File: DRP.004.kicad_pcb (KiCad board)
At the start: 4 copper layers, 55 x 27 mm, 80 parts, among them J1 Batt_conn_3p, J2 USB_C_Receptacle_PowerOnly_6P, J3 Conn_01x03_Pin, J4 Conn_01x05_Pin, J5 Conn_01x03_Pin, J6 Conn_01x03_Pin, Q1 DTC143Z, Q2 AO3400, Q3 DTC143Z, Q4 DMG1012T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

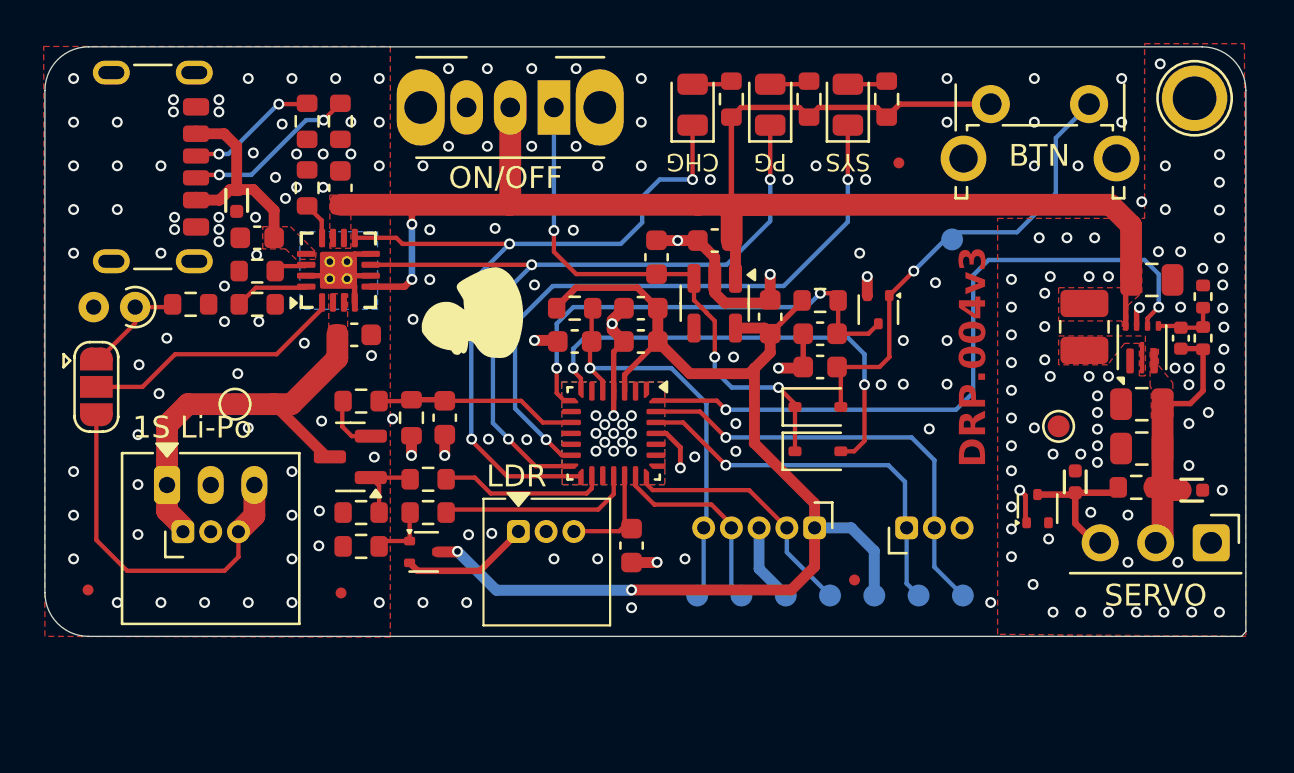
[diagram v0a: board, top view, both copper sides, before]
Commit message: Updated project jobset - Added generation of ibom - Updated production files
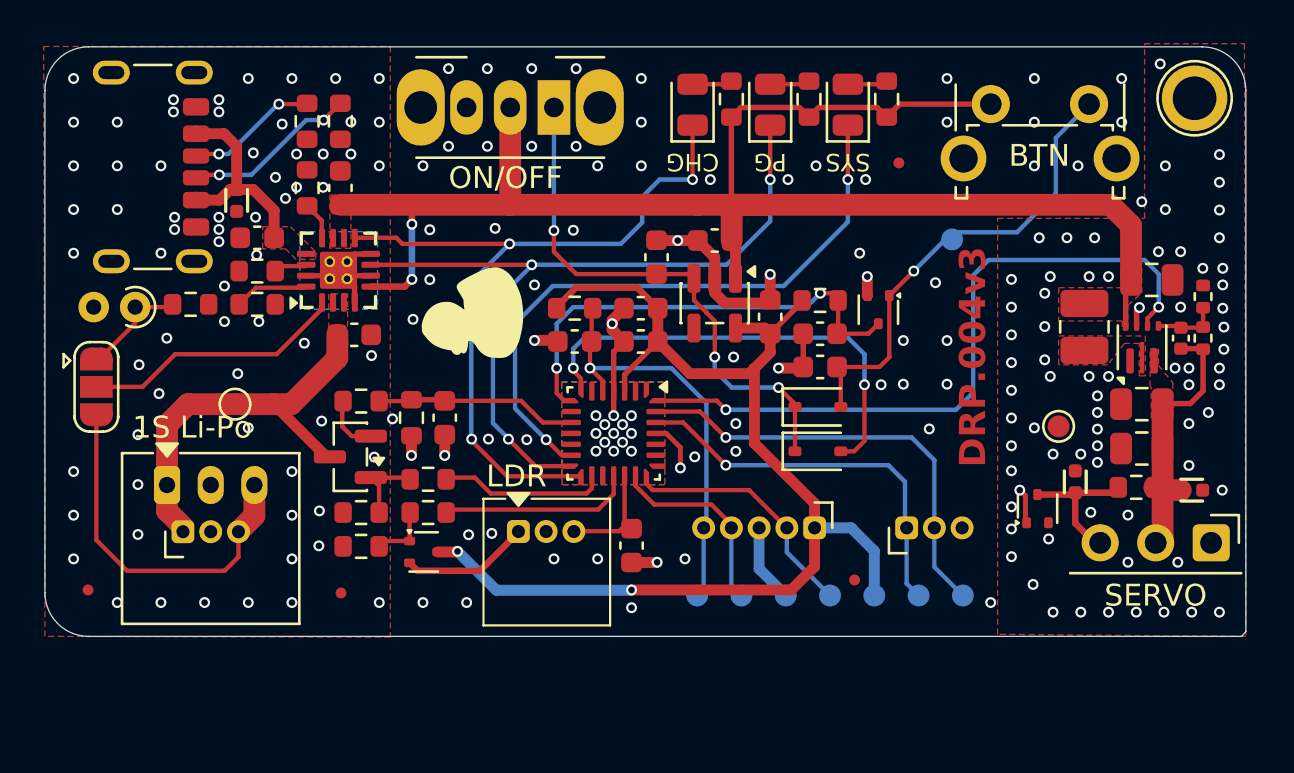
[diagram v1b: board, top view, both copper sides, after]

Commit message: V4 revision - Moved usb to HID side - Changed battery connector to ph2.0 with standard(ish) pinout - Better footprints for debug and ldr connectors - Changed switch from SK12D07 to MSK12C02 - Changed R(ILIM) to 1.1k - Better placement of servo power and connector - Changed thermistor to 0402 SMD - Removed jumper to NTC
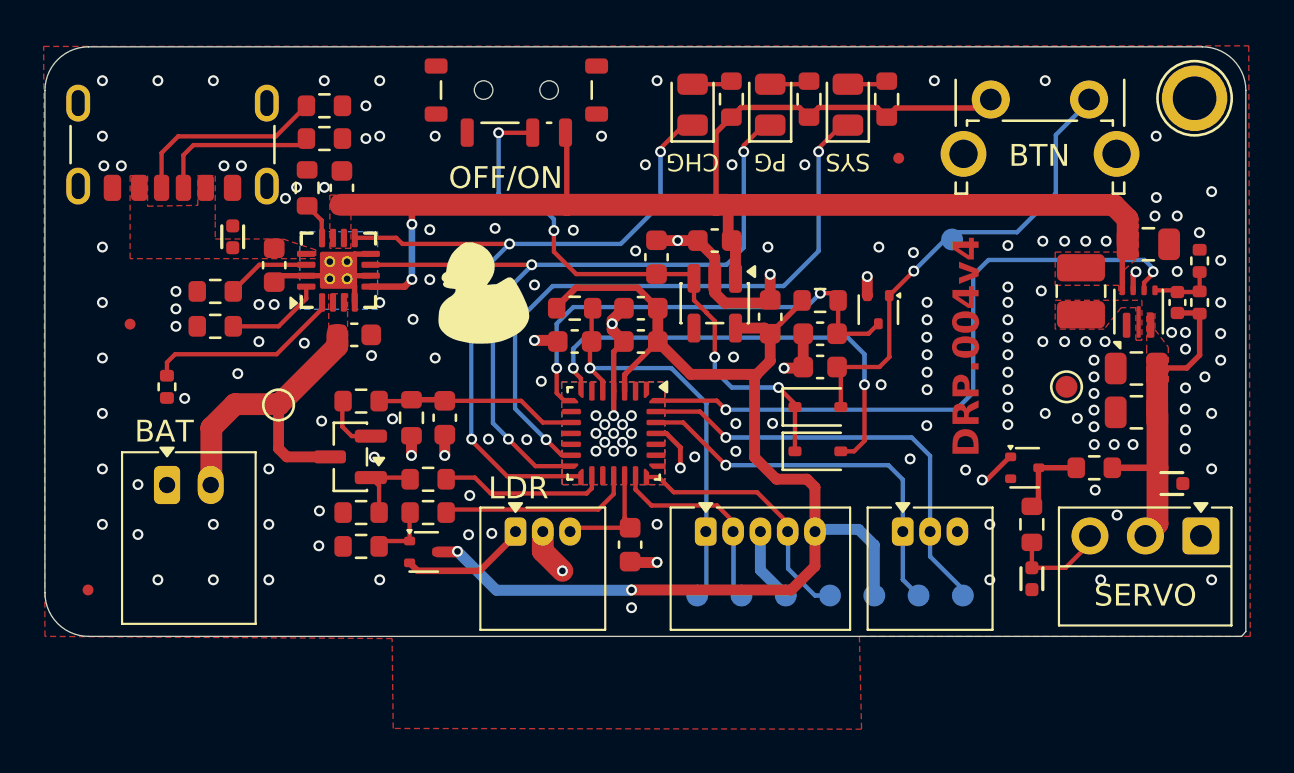
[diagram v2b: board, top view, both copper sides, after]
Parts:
- removed FID4: Fiducial, Fiducial:Fiducial_0.5mm_Mask1.5mm
- removed JP1: SolderJumper_3_Open, Jumper:SolderJumper-3_P1.3mm_Open_RoundedPad1.0x1.5mm
- removed Q1: DTC143Z, Muffin_SMD:SOT-523
- removed SW3: SW_SPDT, Button_Switch_THT:SW_Slide_SPDT_Angled_CK_OS102011MA1Q
- added Q6: DTC143Z, Muffin_SMD:SOT-523, F.Cu at (201.9, 90.3)
- added SW1: SW_SPDT_SH, Muffin_SMD:MSK12C02, F.Cu at (178.6, 73.0)
- J1: value Batt_conn_3p -> Conn_01x02_Pin; footprint Connector_Muffin_THT.pretty:BATTERY_P2+P1.27mm_Horizontal -> Connector_Muffin_THT.pretty:JST_PH_S2B-PH-K_1x02_P2.00mm_Horizontal
- J4: footprint Connector_Muffin_THT.pretty:PinHeader_1x05_P1.27mm_Vertical_clear_silk -> Connector_Muffin_THT.pretty:Molex_PicoBlade_53048-0510_1x05_P1.25mm_Horizontal
- J5: footprint Connector_Muffin_THT.pretty:PinHeader_1x03_P1.27mm_Vertical_clear_silk -> Connector_Muffin_THT.pretty:Molex_PicoBlade_53048-0310_1x03_P1.25mm_Horizontal
- J6: footprint Connector_Muffin_THT.pretty:Connector_JST_1x03_P1.27mm -> Connector_Muffin_THT.pretty:Molex_PicoBlade_53048-0310_1x03_P1.25mm_Horizontal
- R3: value 1.8k -> 1.1k
- R7: value 5.1k -> 100
- R9: value 10k -> 5.1k
- TH1: footprint Resistor_THT:R_Axial_DIN0204_L3.6mm_D1.6mm_P1.90mm_Vertical -> Resistor_SMD:R_0402_1005Metric
- moved R9 42.1 mm to (205.1, 90.3)
- moved FID2 19.4 mm to (196.1, 76.1)
- moved FID3 15.6 mm to (160.9, 83.7)
- moved R7 5.07 mm to (202.2, 92.9), turned to 90 degrees
- moved J4 4.98 mm to (187.3, 93.2), turned to 0 degrees
- moved U3 4.86 mm to (202.2, 95.4), turned to -90 degrees
- moved TH1 3.93 mm to (162.6, 86.6), turned to -90 degrees
- moved J2 2.92 mm to (162.8, 74.4), turned to 180 degrees
- moved R5 2.17 mm to (164.8, 83.8), turned to 180 degrees
- moved R4 2.13 mm to (164.8, 82.2)
- moved TP3 2.00 mm to (167.7, 87.4)
- moved TP7 1.85 mm to (203.8, 86.6)
- moved C3 1.68 mm to (207.0, 87.7)
- moved U4 1.67 mm to (165.6, 79.7), turned to 90 degrees
- moved C4 1.65 mm to (207.0, 85.7)
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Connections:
- J1 pad 1: +BATT -> GND
- J1 pad 2: GND -> +BATT
- J4 pad 1: +1V8 -> NRST
- J4 pad 2: SWCLK -> SWDIO
- J4 pad 4: SWDIO -> SWCLK
- J4 pad 5: NRST -> +1V8
- R7 pad 1: +5V5 -> Net-(J3-Pin_3)
- R7 pad 2: Net-(J3-Pin_3) -> /power/servo_cntrl
- R9 pad 1: GND -> +5V5
- R9 pad 2: Net-(JP1-A) -> /power/servo_cntrl
- TH1 pad 1: Net-(JP1-A) -> Net-(U1-TS)
- U1 pad 1: TS -> Net-(U1-TS)
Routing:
- net Net-(J1-TS): track 16.9 -> 0.00 mm
- net TS: track 11.8 -> 0.00 mm
- net VBUS: track 9.62 -> 0.00 mm
- net Net-(U1-TS): track 0.00 -> 8.73 mm
- net +BATT: track 19.7 -> 14.8 mm
- net Net-(JP1-A): track 4.77 -> 0.00 mm
- net VSYS: track 72.4 -> 68.3 mm
- net /power/servo_cntrl: track 0.00 -> 3.45 mm
- net Net-(U1-TMR): track 1.22 -> 3.84 mm
- net EN_SYS: track 24.2 -> 26.5 mm, vias 3 -> 4
- net +5V5: track 12.8 -> 14.7 mm
- net EN_SERVO: track 32.0 -> 30.2 mm
- net Net-(J3-Pin_3): track 6.15 -> 4.63 mm
- net Net-(J2-CC1): track 5.95 -> 7.45 mm, vias 2 -> 0
- net SERVO_PWM: track 19.9 -> 18.5 mm
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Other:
- board text added: "BAT"
- board text added: "OFF/ON"
- board text removed: "1S Li-Po"
- board text removed: "ON/OFF"

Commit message: v4.1 - Changed SW2 to SMT (with lower profile) - Widen annular ring of vias - Small changes in routing (due to wider vias)
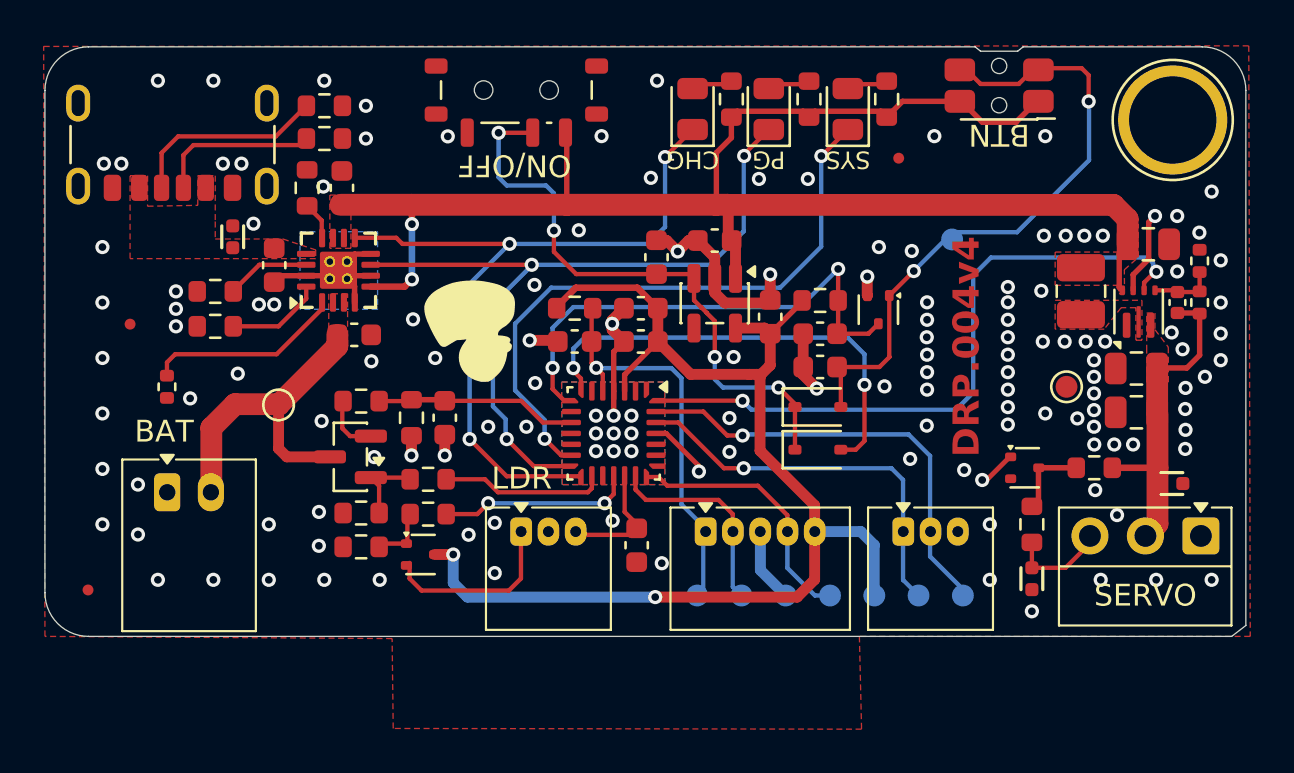
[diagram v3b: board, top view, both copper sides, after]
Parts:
- C16, C9: value 10nF -> 1nF
- R20, R21, R23: value 220 -> 1.1k
- SW2: footprint Button_Switch_THT:SW_Tactile_SPST_Angled_PTS645Vx58-2LFS -> Button_Switch_SMD:SW_SPST_EVQP7C
- TP6: footprint TestPoint:TestPoint_Plated_Hole_D2.0mm -> TestPoint:TestPoint_Plated_Hole_D4.0mm
- moved #G1 1.86 mm to (176.4, 84.0), turned to 180 degrees
- moved TP6 1.41 mm to (208.7, 74.3)
- moved SW2 0.74 mm to (200.7, 72.8), turned to 180 degrees
- moved J1 0.33 mm to (162.6, 91.4)
- moved C16 0.30 mm to (184.1, 93.8)
- moved J6 0.26 mm to (178.8, 93.2)
- moved D4 0.21 mm to (190.2, 73.8)
- moved D3 0.20 mm to (186.7, 73.8)
- moved D5 0.20 mm to (193.8, 73.8)
- moved Q4 0.19 mm to (174.2, 94.2)
- moved D1 0.07 mm to (192.4, 89.5)
- moved R22 0.07 mm to (174.6, 92.4)
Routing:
- net /control/SWITCH: track 21.2 -> 28.9 mm, vias 1 -> 2
- net VSYS: track 68.3 -> 71.2 mm
- net Net-(J6-Pin_1): track 5.86 -> 8.76 mm
- net ON_DETECT: track 20.8 -> 22.7 mm
- net +1V8: track 55.4 -> 56.6 mm
- net ADC_LDR: track 4.93 -> 5.91 mm
- net PGOOD: track 36.1 -> 35.2 mm
- net CHRG: track 34.4 -> 35.1 mm
- net GND: track 34.1 -> 34.7 mm, vias 169 -> 141
- net SWDIO: track 8.87 -> 9.45 mm
- net EN_LDR: track 8.75 -> 8.90 mm, vias 0 -> 2
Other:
- outline, holes or cut-outs redrawn
- board text added: "ON/OFF"
- board text removed: "OFF/ON"

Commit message: v4.2 Revision - Rerouting again - New SW2
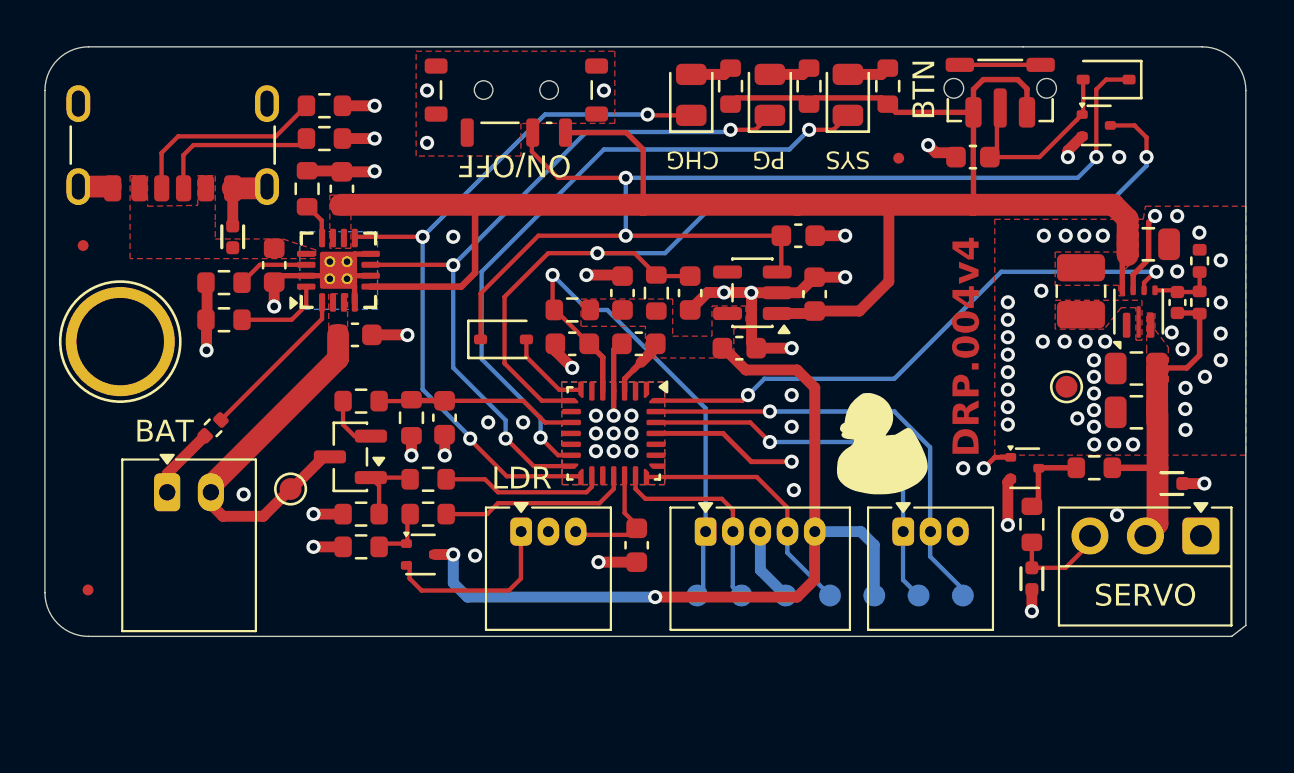
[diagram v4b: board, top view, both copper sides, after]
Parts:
- removed TP11: TestPoint, TestPoint:TestPoint_Pad_D1.0mm
- SW2: footprint Button_Switch_SMD:SW_SPST_EVQP7C -> Muffin_SMD:SW_Push_1P1T-MP_NO_Horizontal_Alps_SKRTLAE010
- moved TP6 49.3 mm to (160.4, 84.5)
- moved D2 20.0 mm to (205.6, 72.5), turned to 180 degrees
- moved #G1 19.7 mm to (195.4, 89.2), turned to 0 degrees
- moved D1 15.3 mm to (178.0, 84.4)
- moved Q3 13.1 mm to (205.2, 74.6), turned to 0 degrees
- moved C11 11.9 mm to (199.5, 76.0)
- moved R18 7.51 mm to (185.0, 82.3), turned to -90 degrees
- moved C7 6.57 mm to (191.5, 79.7), turned to 180 degrees
- moved C10 6.24 mm to (186.6, 82.3), turned to -90 degrees
- moved C5 5.19 mm to (192.2, 82.3), turned to 90 degrees
- moved FID3 4.19 mm to (158.8, 80.1)
- moved TP3 3.89 mm to (168.2, 91.2)
- moved TH1 2.83 mm to (164.7, 88.5), turned to -135 degrees
- moved C17 2.02 mm to (188.8, 84.8), turned to 0 degrees
- moved U7 1.79 mm to (189.4, 82.3), turned to 180 degrees
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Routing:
- net GND: track 34.7 -> 67.8 mm, vias 141 -> 86
- net EN_SYS: track 27.0 -> 53.8 mm, vias 4 -> 3
- net ON_DETECT: track 22.7 -> 46.8 mm
- net /control/SWITCH: track 28.9 -> 9.14 mm, vias 2 -> 0
- net ON_LATCH: track 21.1 -> 4.18 mm, vias 2 -> 0
- net +1V8: track 56.6 -> 41.7 mm
- net VSYS: track 71.2 -> 84.8 mm, vias 2 -> 0
- net NRST: track 18.6 -> 24.5 mm
- net EN_SERVO: track 30.6 -> 26.4 mm
- net unconnected-(SW2-B-PadSH)_1: track 0.00 -> 3.70 mm
- net Net-(U1-TS): track 8.73 -> 7.01 mm
- net +BATT: track 14.8 -> 16.5 mm
- net PGOOD: track 35.2 -> 33.6 mm
- net LED_RED: track 28.7 -> 30.2 mm
- net CHRG: track 35.1 -> 33.7 mm
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- added copper zone on F.Cu, net +1V8
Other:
- outline, holes or cut-outs redrawn

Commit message: v4.3 - Smaller, faster, stronger (lol) - Removed few appendixes - Updated doc jobs set
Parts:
- removed D2: 1N4148WS, Diode_SMD:D_SOD-323
- removed Q2: AO3400, Package_TO_SOT_SMD:SOT-23
- removed R13: 10k, Resistor_SMD:R_0603_1608Metric
- removed R8: 100k, Resistor_SMD:R_0603_1608Metric
- removed TP6: TestPoint, TestPoint:TestPoint_Plated_Hole_D4.0mm
- added Q1: AO3400A, Package_TO_SOT_SMD:SOT-23, F.Cu at (166.2, 90.2)
- R1: value 100k -> 10k
- R20, R21, R23: value 1.1k -> 3.3k
- TP1: value TestPoint -> U_TX
- TP2: value TestPoint -> U_RX
- TP3: value TestPoint -> VBAT
- TP4: value TestPoint -> SWDIO
- TP5: value TestPoint -> ~{NRST}
- TP7, TP8: value TestPoint -> GND
- TP9: value TestPoint -> SWCLK
- moved FID1 30.0 mm to (186.0, 82.8)
- moved C7 16.9 mm to (174.9, 76.6), turned to 0 degrees
- moved FID2 15.6 mm to (180.5, 75.8)
- moved Q6 13.9 mm to (188.0, 90.8)
- moved TP7 13.2 mm to (190.5, 86.3)
- moved J3 13.2 mm to (196.8, 93.6)
- moved C18 13.2 mm to (195.7, 82.7)
- moved C2 13.2 mm to (194.4, 80.0)
- moved C3 13.2 mm to (193.8, 87.7)
- moved C4 13.2 mm to (193.8, 85.7)
- moved L1 13.2 mm to (191.3, 82.2)
- moved R2 13.2 mm to (196.7, 80.8)
- moved R6 13.2 mm to (196.7, 82.7)
- moved U2 13.2 mm to (195.5, 91.0)
- moved U5 13.2 mm to (193.9, 83.1)
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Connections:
- J3 pad 3: Net-(J3-Pin_3) -> /power/servo_cntrl
- Q6 pad 3: /power/servo_cntrl -> Net-(Q6-C)
- R1 pad 1: Net-(Q4-G) -> EN_LOAD_BATT
- R1 pad 2: GND -> Net-(Q1-G)
- R7 pad 1: Net-(J3-Pin_3) -> /power/servo_cntrl
- R7 pad 2: /power/servo_cntrl -> Net-(Q6-C)
- R9 pad 2: /power/servo_cntrl -> Net-(Q6-C)
- U3 pad 1: Net-(J3-Pin_3) -> /power/servo_cntrl
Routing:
- net EN_SYS: track 53.8 -> 17.9 mm, vias 3 -> 2
- net VSYS: track 84.8 -> 66.9 mm, vias 0 -> 2
- net EN_SERVO: track 26.4 -> 20.2 mm
- net SERVO_PWM: track 18.0 -> 11.8 mm
- net +BATT: track 16.5 -> 10.4 mm
- net /control/SWITCH: track 9.14 -> 3.29 mm
- net Net-(J6-Pin_1): track 8.76 -> 3.23 mm
- net GND: track 67.8 -> 62.4 mm, vias 86 -> 254
- net NRST: track 24.5 -> 19.6 mm
- net USART_RX: track 20.4 -> 15.6 mm
- net Net-(J3-Pin_3): track 4.63 -> 0.00 mm
- net USART_TX: track 18.5 -> 14.2 mm
- net unconnected-(SW2-B-PadSH): track 3.70 -> 0.00 mm
- net +1V8: track 41.7 -> 38.0 mm, vias 2 -> 0
- net Net-(Q2-G): track 3.38 -> 0.00 mm
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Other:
- board size 55 x 27 mm -> 42 x 27 mm
- board text added: "0.3000 mm"
- board text added: "42.0000 mm x 27.0000 mm"
- board text removed: "0.2500 mm"
- board text removed: "55.0000 mm x 27.0000 mm"
- board text removed: "SYS"

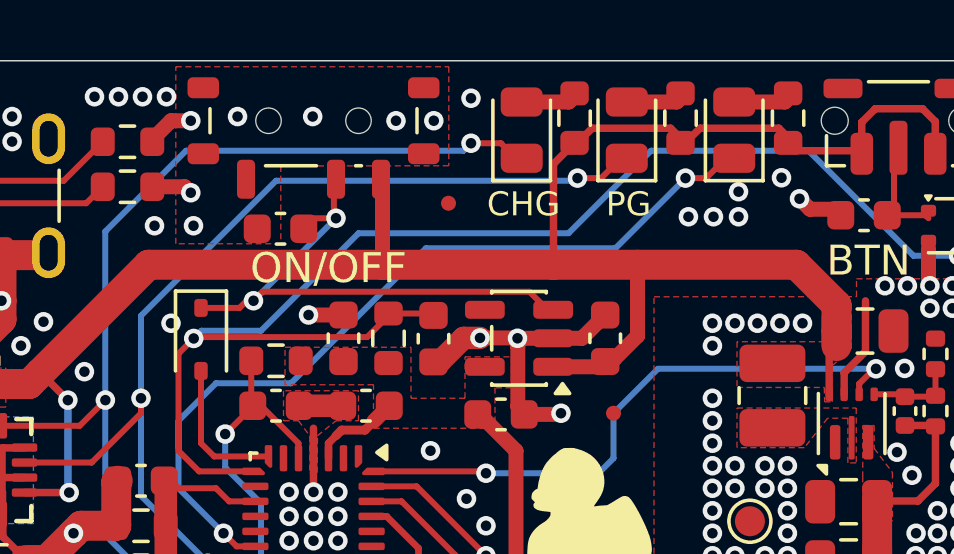
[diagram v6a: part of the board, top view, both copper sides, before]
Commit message: Updated release project to new flow
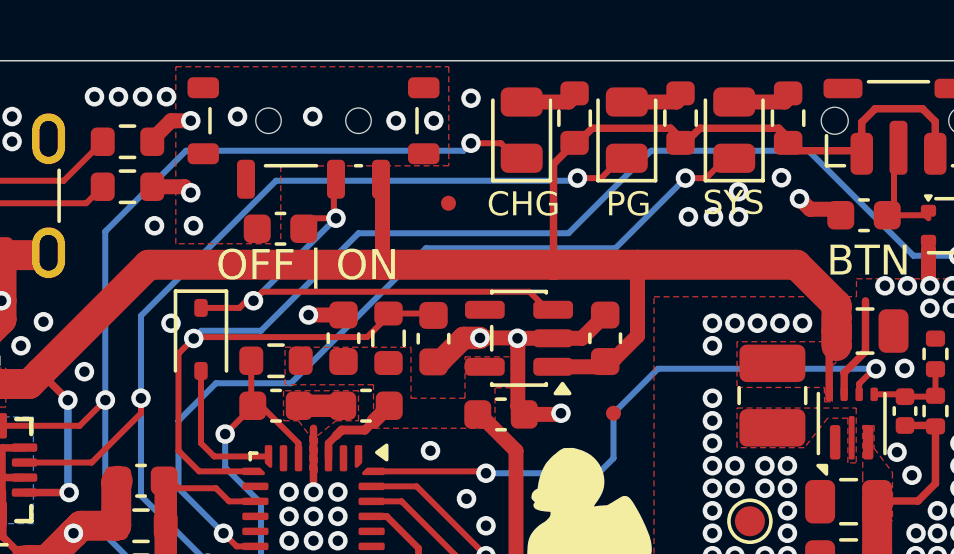
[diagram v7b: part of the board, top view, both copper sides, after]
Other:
- board text added: "OFF | ON"
- board text added: "SYS"
- board text removed: "ON/OFF"
